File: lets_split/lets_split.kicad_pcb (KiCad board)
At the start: 2 copper layers, 112 x 79 mm, 62 parts, among them J1 3PIN, J2 6PIN, J3 3PIN, SW1 SW_PUSH, SW10 SW_PUSH, SW11 SW_PUSH, SW12 SW_PUSH, SW13 SW_PUSH, SW14 SW_PUSH, SW15 SW_PUSH, SW16 SW_PUSH, SW17 SW_PUSH, SW18 SW_PUSH, SW19 SW_PUSH, SW2 SW_PUSH, SW21 SW_PUSH, SW22 SW_PUSH, SW23 SW_PUSH, SW3 SW_PUSH, SW4 SW_PUSH, SW5 SW_PUSH, SW6 SW_PUSH, SW7 SW_PUSH, SW8 SW_PUSH, SW9 SW_PUSH, U2 HOLE, U3 HOLE, U4 HOLE, U5 HOLE

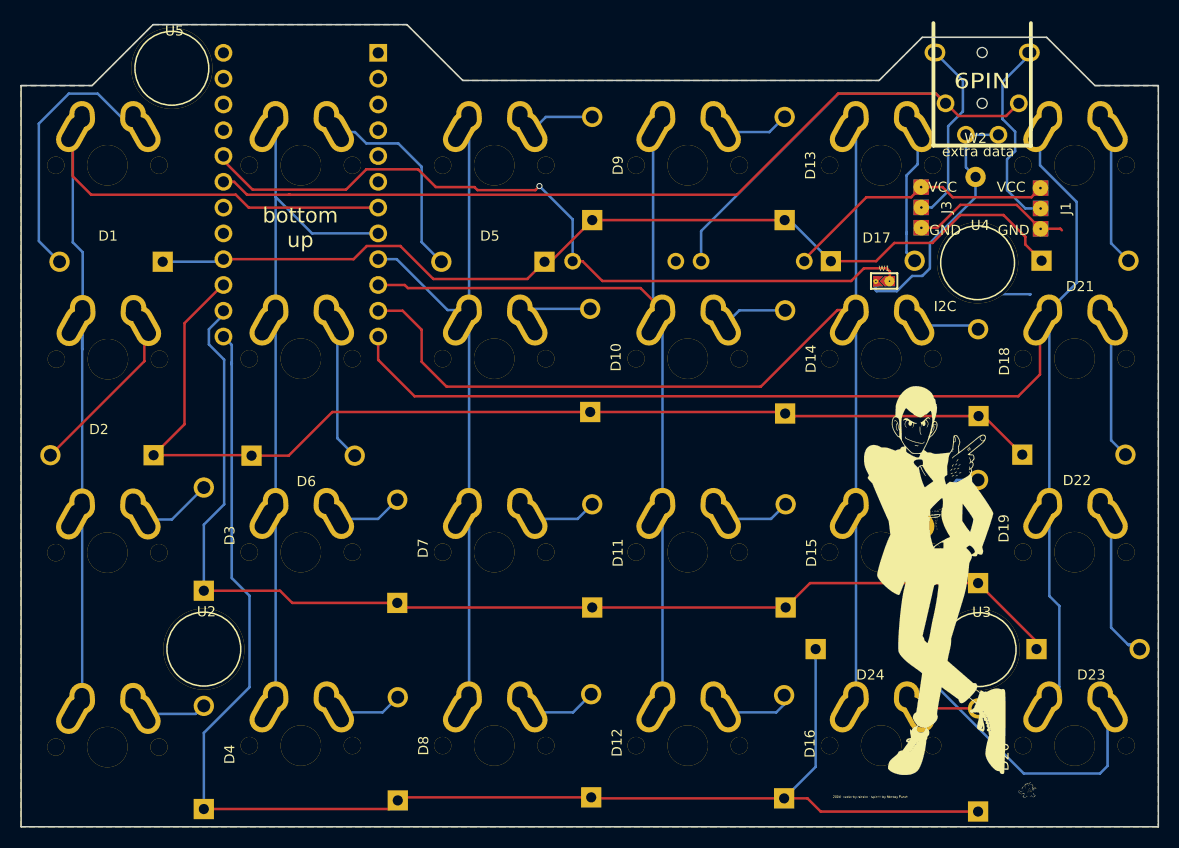
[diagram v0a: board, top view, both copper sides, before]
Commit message: Change controller ProMicro to MCP23017
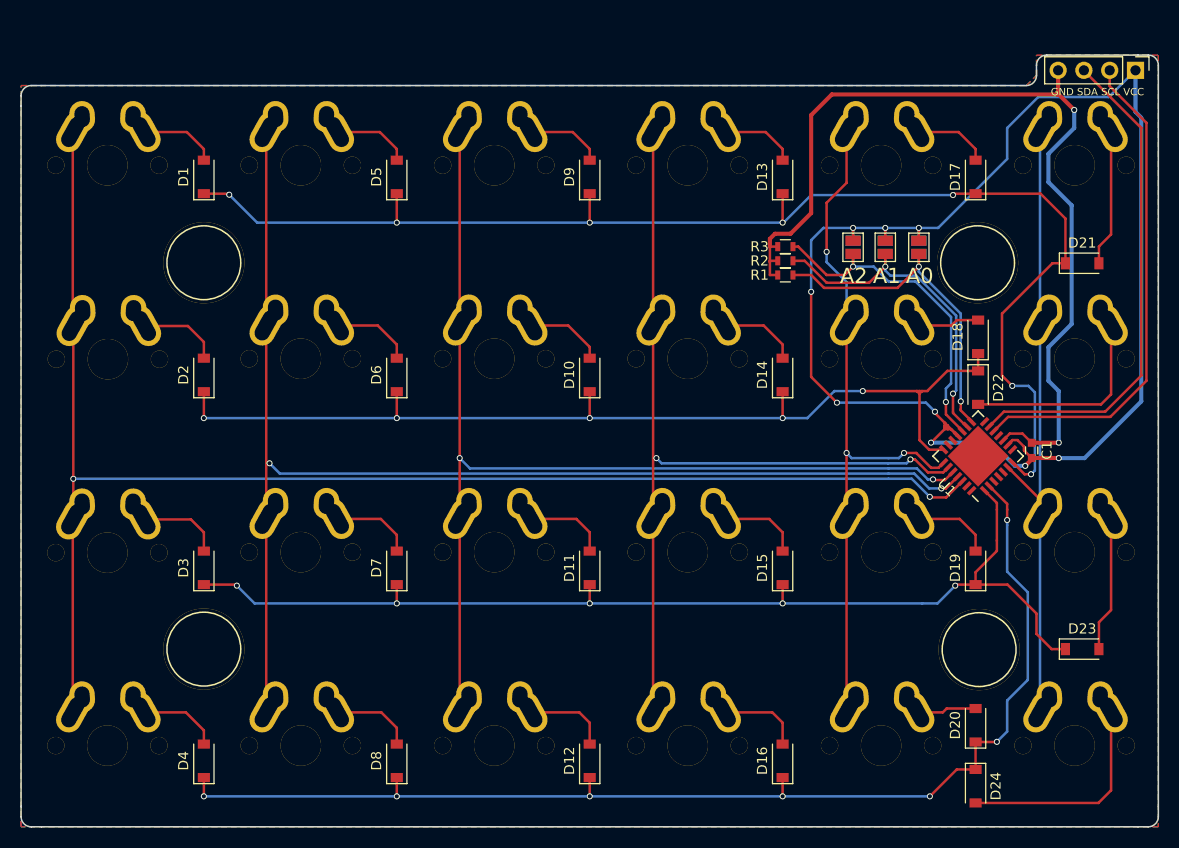
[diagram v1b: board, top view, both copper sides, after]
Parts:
- removed ? (x2): SW_PUSH, flipalps:MXALPS_FLIP
- removed G*** (x2): LOGO, LOGO
- removed J1: 3PIN, prettylib:jumper
- removed J2: 6PIN, footprint:4pin35mmAudio
- removed W1: TEST, prettylib:JUMPER_SMD_2DUB
- removed W2: TEST_1P, Wire_Pads:SolderWirePad_single_2mmDrill
- added C1: 0.1u, Capacitors_SMD:C_0603, F.Cu at (136.5, 74.9)
- added JP1: Jumper_NO_Small, Jumper:SolderJumper-2_P1.3mm_Open_Pad1.0x1.5mm, F.Cu at (125.4, 54.9)
- added JP2: Jumper_NO_Small, Jumper:SolderJumper-2_P1.3mm_Open_Pad1.0x1.5mm, F.Cu at (122.1, 54.9)
- added JP3: Jumper_NO_Small, Jumper:SolderJumper-2_P1.3mm_Open_Pad1.0x1.5mm, F.Cu at (118.9, 54.9)
- added JP4: Jumper_NO_Small, Jumper:SolderJumper-2_P1.3mm_Open_Pad1.0x1.5mm, B.Cu at (125.4, 54.9)
- added JP5: Jumper_NO_Small, Jumper:SolderJumper-2_P1.3mm_Open_Pad1.0x1.5mm, B.Cu at (122.1, 54.9)
- added JP6: Jumper_NO_Small, Jumper:SolderJumper-2_P1.3mm_Open_Pad1.0x1.5mm, B.Cu at (118.9, 54.9)
- added R3: 10k, Resistors_SMD:R_0603, F.Cu at (112.3, 54.9)
- added SW20: SW_PUSH, flipalps:MXALPS_FLIP, F.Cu at (121.7, 104.0)
- added SW24: SW_PUSH, flipalps:MXALPS_FLIP, F.Cu at (140.8, 104.0)
- D1, D10, D11, D12, D13, D14, D15, D16, D17, D18, D19, D2, D20, D21, D22, D23, D24, D3, D4, D5, D6, D7, D8, D9: footprint Diodes_ThroughHole:Diode_DO-41_SOD81_Horizontal_RM10 -> Diodes_SMD:D_SOD-123
- J3: value 3PIN -> Conn_01x04; footprint prettylib:jumper -> Pin_Headers:Pin_Header_Straight_1x04_Pitch2.54mm
- R1, R2: value R -> 10k; footprint footprint:RESISTOR -> Resistors_SMD:R_0603; moved to F.Cu
- U1: value (none) -> MCP23017; footprint footprint:TEENSY_2.0 -> Housings_DFN_QFN:QFN-28-1EP_6x6mm_Pitch0.65mm; moved to F.Cu
- moved U1 71.5 mm to (131.2, 75.5), turned to 135 degrees
- moved J3 23.4 mm to (146.8, 37.5), turned to 270 degrees
- moved D24 20.7 mm to (131.0, 108.0), turned to 270 degrees
- moved U5 19.4 mm to (56.6, 57.1)
- moved D5 16.8 mm to (74.0, 48.0), turned to 90 degrees
- moved D17 16.5 mm to (131.0, 48.0), turned to 90 degrees
- moved D6 16.4 mm to (74.0, 67.5), turned to 90 degrees
- moved R1 15.9 mm to (112.3, 57.7)
- moved D2 9.32 mm to (55.0, 67.5), turned to 90 degrees
- moved D1 9.28 mm to (55.0, 48.0), turned to 90 degrees
- moved D20 8.50 mm to (131.0, 102.0)
- moved D22 7.90 mm to (131.2, 68.8), turned to 270 degrees
- moved D18 7.80 mm to (131.2, 63.8)
- moved D21 5.61 mm to (141.5, 56.5)
- moved D4 4.75 mm to (55.0, 105.5)
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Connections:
- J3 pad 1: GND -> VCC
- J3 pad 2: Net-(J2-Pad4) -> Net-(J3-Pad2)
- J3 pad 3: VCC -> Net-(J3-Pad3)
- R1 pad 1: VCC -> Net-(JP1-Pad1)
- R1 pad 2: Net-(R1-Pad2) -> GND
- R2 pad 1: data -> Net-(JP2-Pad1)
- R2 pad 2: VCC -> GND
- U1 pad 1: Net-(U1-Pad1) -> row2
- U1 pad 10: col3 -> GND
- U1 pad 11: col4 -> (no net)
- U1 pad 12: col5 -> Net-(J3-Pad2)
- U1 pad 18: row3 -> VCC
- U1 pad 19: row2 -> (no net)
- U1 pad 2: GND -> row3
- U1 pad 20: row1 -> (no net)
- U1 pad 21: row0 -> row1
- U1 pad 22: Net-(U1-Pad22) -> col4
- U1 pad 23: Net-(U1-Pad23) -> col3
- U1 pad 24: data -> col2
- U1 pad 25: Net-(R1-Pad2) -> col1
- U1 pad 26: GND -> col0
- U1 pad 27: GND -> (no net)
- U1 pad 28: Net-(U1-Pad28) -> (no net)
- U1 pad 29: Net-(U1-Pad29) -> (no net)
- U1 pad 3: Net-(U1-Pad3) -> (no net)
- U1 pad 4: VCC -> (no net)
- U1 pad 5: Net-(U1-Pad5) -> (no net)
- U1 pad 6: Net-(U1-Pad6) -> col5
- U1 pad 7: col0 -> row0
- U1 pad 8: col1 -> (no net)
- U1 pad 9: col2 -> VCC
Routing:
- net VCC: track 27.2 -> 145.0 mm, vias 0 -> 9
- net data: track 117.5 -> 0.00 mm
- net Net-(R1-Pad2): track 77.0 -> 0.00 mm, vias 1 -> 0
- net GND: track 15.8 -> 92.8 mm, vias 0 -> 2
- net col5: track 133.7 -> 62.7 mm
- net col1: track 68.7 -> 126.8 mm, vias 0 -> 2
- net col0: track 96.5 -> 146.2 mm, vias 0 -> 2
- net Net-(J3-Pad3): track 0.00 -> 49.5 mm
- net Net-(J3-Pad2): track 0.00 -> 49.2 mm
- net col4: track 112.3 -> 69.6 mm, vias 0 -> 3
- net col2: track 68.2 -> 107.0 mm, vias 0 -> 2
- net Net-(JP2-Pad1): track 0.00 -> 34.0 mm, vias 0 -> 2
- net Net-(JP3-Pad1): track 0.00 -> 33.7 mm, vias 0 -> 2
- net Net-(JP1-Pad1): track 0.00 -> 33.7 mm, vias 0 -> 2
- net row0: track 96.8 -> 130.1 mm, vias 0 -> 7
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- added copper zone on B.Cu, net GND
- removed copper zone on B.Cu, net VCC
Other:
- board size 112 x 79 mm -> 112 x 76 mm
- net class Bold added: clearance 0.2, trace_width 0.4064, via_dia 0.6, via_drill 0.4
- board text added: "A0"
- board text added: "A1"
- board text added: "A2"
- board text added: "GND SDA SCL VCC"
- board text added: "VCC SCL SDA GND"
- board text removed: "By Wootpatoot"
- board text removed: "GND"
- board text removed: "I2C"
- board text removed: "LET'S SPLIT"
- board text removed: "VCC"
- board text removed: "bottom up"
- board text removed: "extra data"
- board text removed: "top up"
